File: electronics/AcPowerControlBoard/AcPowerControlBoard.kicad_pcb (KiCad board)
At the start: 2 copper layers, 10 x 10 mm, 1 part

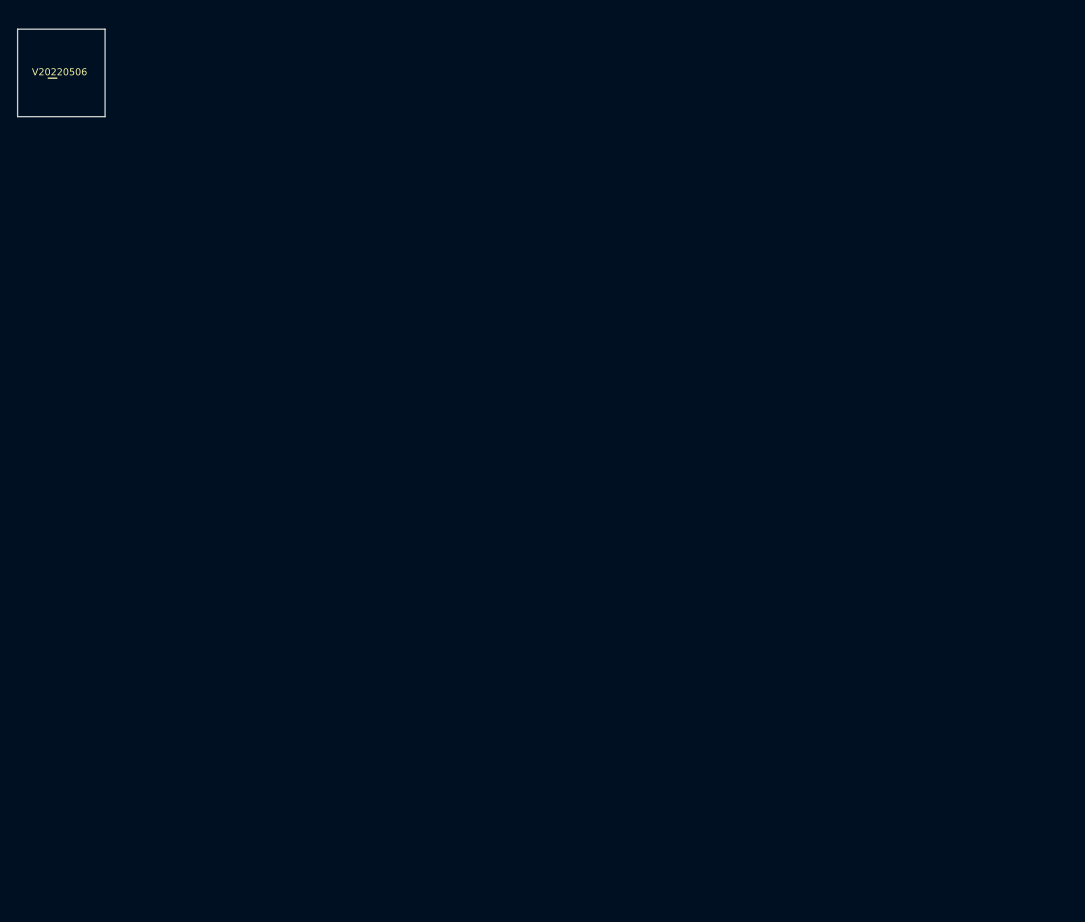
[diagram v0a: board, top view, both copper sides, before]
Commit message: added safety relay and rectifier subsystem
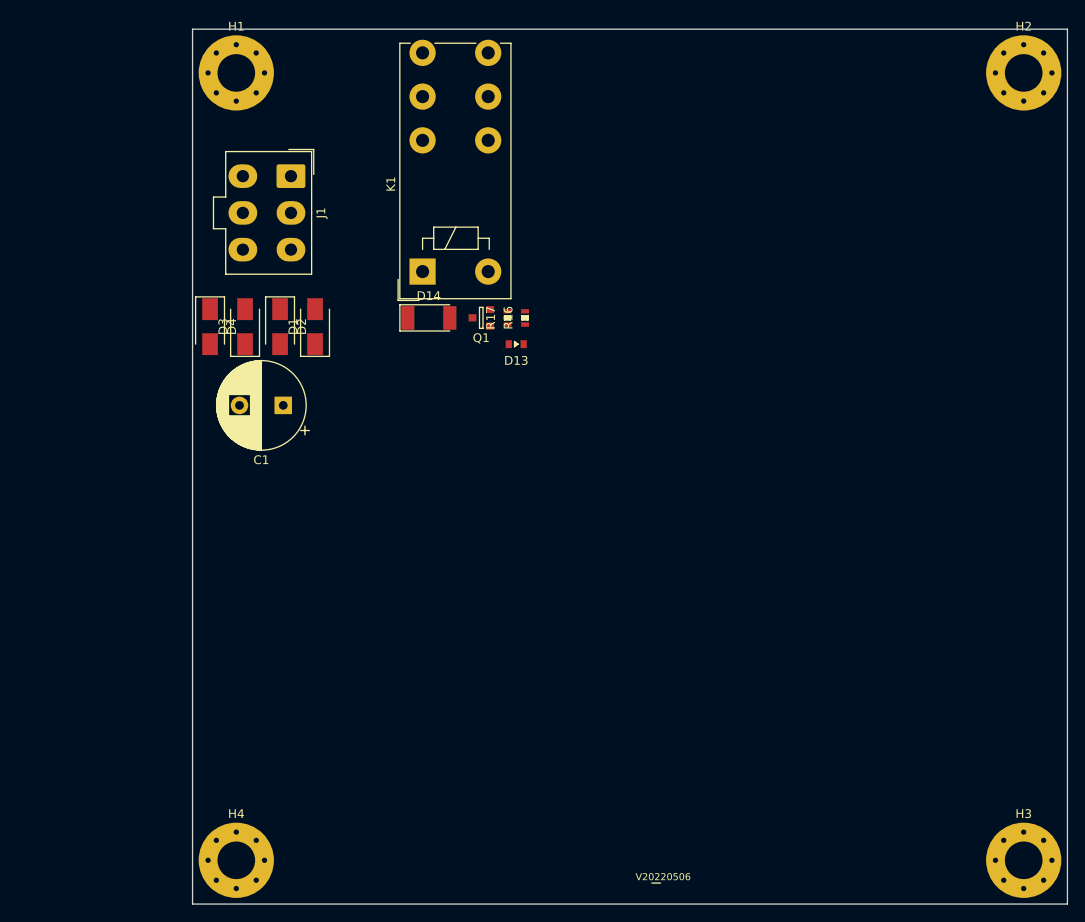
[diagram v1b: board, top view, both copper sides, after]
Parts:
- added C1: 470u, Capacitor_THT:CP_Radial_D10.0mm_P5.00mm, F.Cu at (50.4, 63.0)
- added D1: 1N4001, Diode_SMD:D_SMA, F.Cu at (54.0, 54.0)
- added D13: LED, SquantorDiodes:LED_0603_hand, F.Cu at (77.0, 56.0)
- added D14: LL4148, Diode_SMD:D_MELF, F.Cu at (67.0, 53.0)
- added D2: 1N4001, Diode_SMD:D_SMA, F.Cu at (50.0, 54.0)
- added D3: 1N4001, Diode_SMD:D_SMA, F.Cu at (46.0, 54.0)
- added D4: 1N4001, Diode_SMD:D_SMA, F.Cu at (42.0, 54.0)
- added H1: M4, MountingHole:MountingHole_4.3mm_M4_Pad_Via, F.Cu at (45.0, 25.0)
- added H2: M4, MountingHole:MountingHole_4.3mm_M4_Pad_Via, F.Cu at (135.0, 25.0)
- added H3: M4, MountingHole:MountingHole_4.3mm_M4_Pad_Via, F.Cu at (135.0, 115.0)
- added H4: M4, MountingHole:MountingHole_4.3mm_M4_Pad_Via, F.Cu at (45.0, 115.0)
- added J1: molex microfit, Connector_Molex:Molex_Mini-Fit_Jr_5566-06A_2x03_P4.20mm_Vertical, F.Cu at (51.2, 36.8)
- added K1: FINDER-40.52, Relay_THT:Relay_DPDT_Finder_40.52, F.Cu at (66.3, 47.7)
- added Q1: Q_NMOS_GSD, SquantorIC:SOT23-3, F.Cu at (73.0, 53.0)
- added R16: 1K, SquantorRcl:R_0603, F.Cu at (78.0, 53.0)
- added R17: 10K, SquantorRcl:R_0603, F.Cu at (76.0, 53.0)
- moved N1 115.0 mm to (93.0, 117.0)
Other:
- board size 10 x 10 mm -> 100 x 100 mm
